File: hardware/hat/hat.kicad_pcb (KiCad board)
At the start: 4 copper layers, 65 x 56 mm, 83 parts, among them J1 GPIO, J2 Uart, J3 LineIn, J4 LineOut, J5 Headphone, U1 CAT24C256, U2 TPS7A20xxxDBV, U3 Oled, U4 MAX98089ETN_T, Y1 12.288MHz

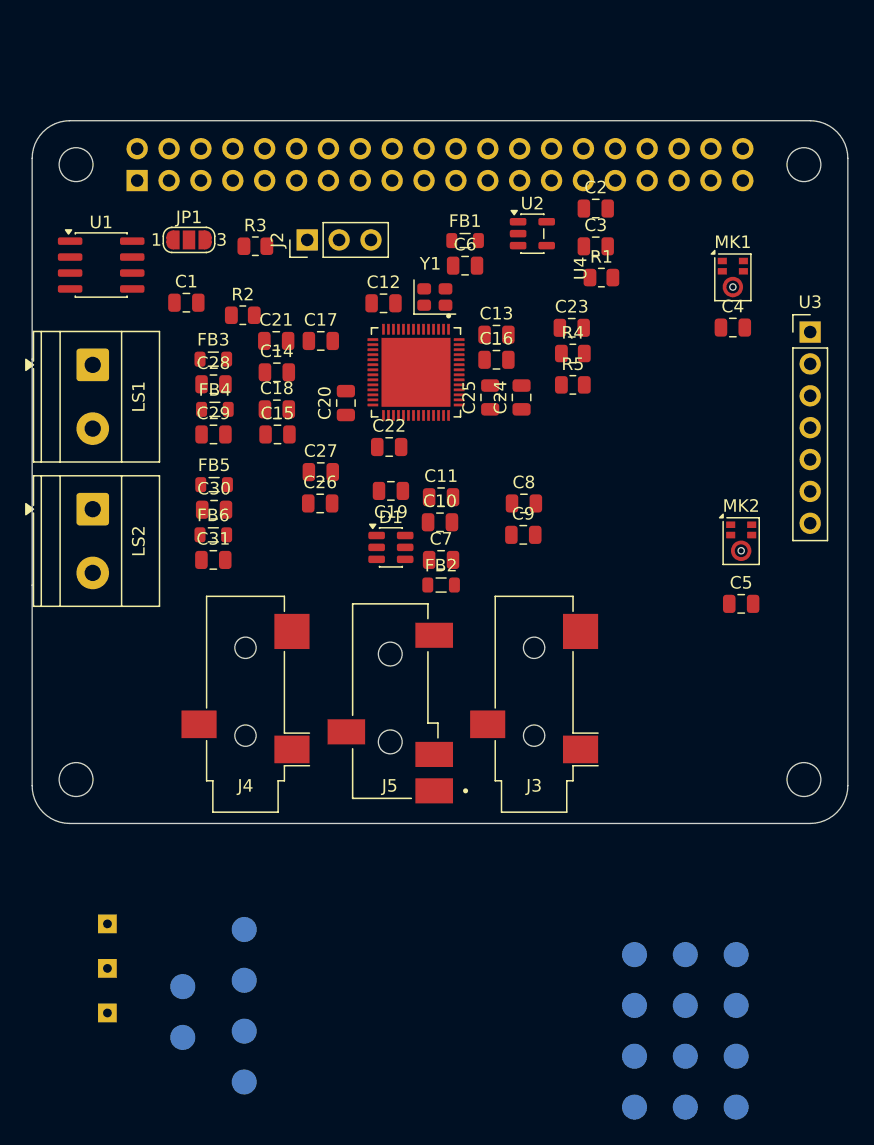
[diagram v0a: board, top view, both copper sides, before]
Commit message: bypass cap
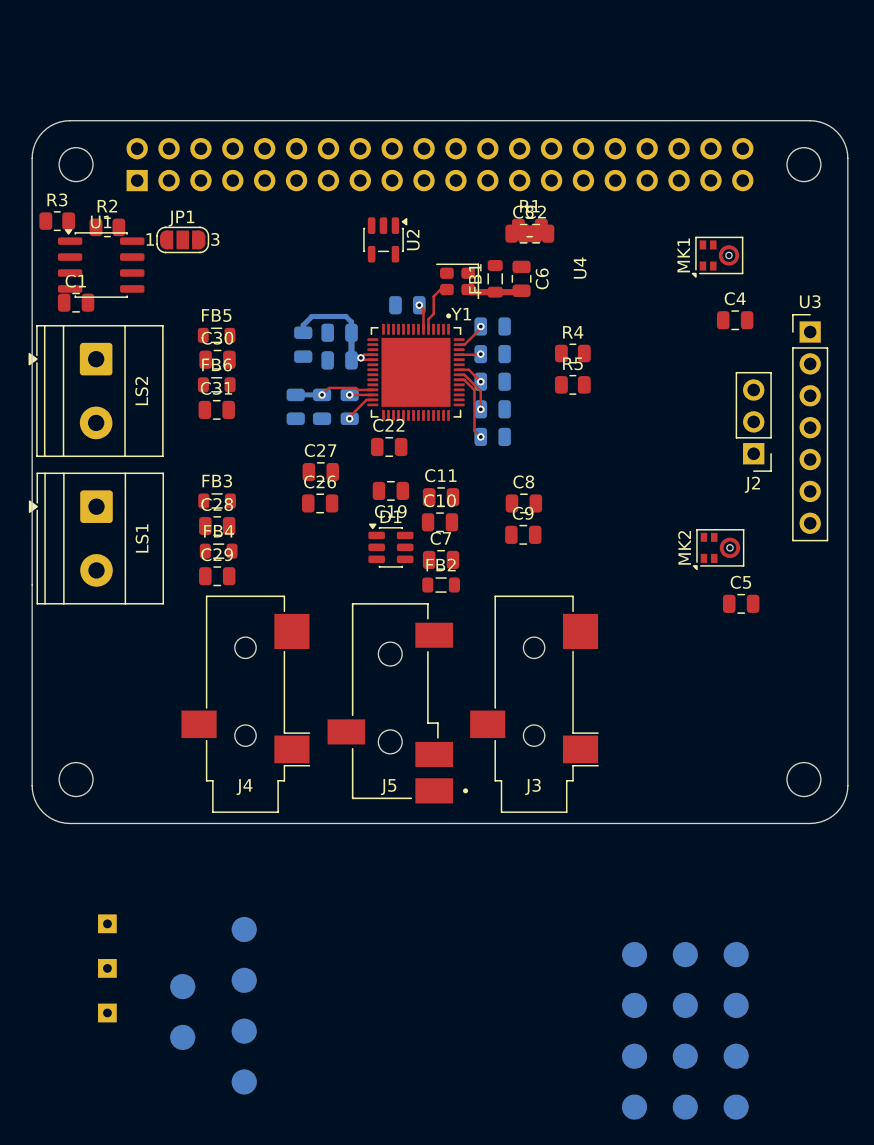
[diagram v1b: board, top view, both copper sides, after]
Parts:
- C12, C13, C14, C15, C16, C17, C18, C20, C21, C23, C24, C25: moved to B.Cu
- moved J2 39.4 mm to (157.5, 70.5), turned to 180 degrees
- moved R3 15.9 mm to (102.0, 52.0)
- moved R2 12.9 mm to (106.0, 52.5)
- moved C30 12.0 mm to (114.8, 63.0)
- moved C31 12.0 mm to (114.7, 67.0)
- moved FB6 12.0 mm to (114.7, 65.0)
- moved LS2 12.0 mm to (105.1, 63.0)
- moved FB5 11.9 mm to (114.7, 61.1)
- moved U2 11.9 mm to (128.0, 53.5), turned to -90 degrees
- moved C28 11.3 mm to (114.8, 76.3)
- moved C29 11.3 mm to (114.8, 80.3)
- moved FB3 11.3 mm to (114.7, 74.3)
- moved FB4 11.3 mm to (114.9, 78.3)
- moved LS1 11.3 mm to (105.1, 74.8)
- moved C1 8.79 mm to (103.5, 58.5)
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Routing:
- net +5V: track 0.00 -> 10.9 mm, vias 0 -> 1
- net +1V8: track 0.00 -> 10.3 mm, vias 0 -> 3
- net Net-(U4-REF): track 0.00 -> 5.50 mm, vias 0 -> 1
- net +3V3: track 0.00 -> 4.47 mm, vias 0 -> 2
- net Net-(Y1-Vcc): track 0.00 -> 4.38 mm
- net Net-(U4-MCLK): track 0.00 -> 4.06 mm
- net Net-(U4-REG): track 0.00 -> 3.72 mm, vias 0 -> 1
- net /codec/C1N: track 0.00 -> 2.56 mm, vias 0 -> 1
- net /codec/C1P: track 0.00 -> 1.85 mm, vias 0 -> 1
- added copper zone on In1.Cu, net GND

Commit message: all signal except ID chip
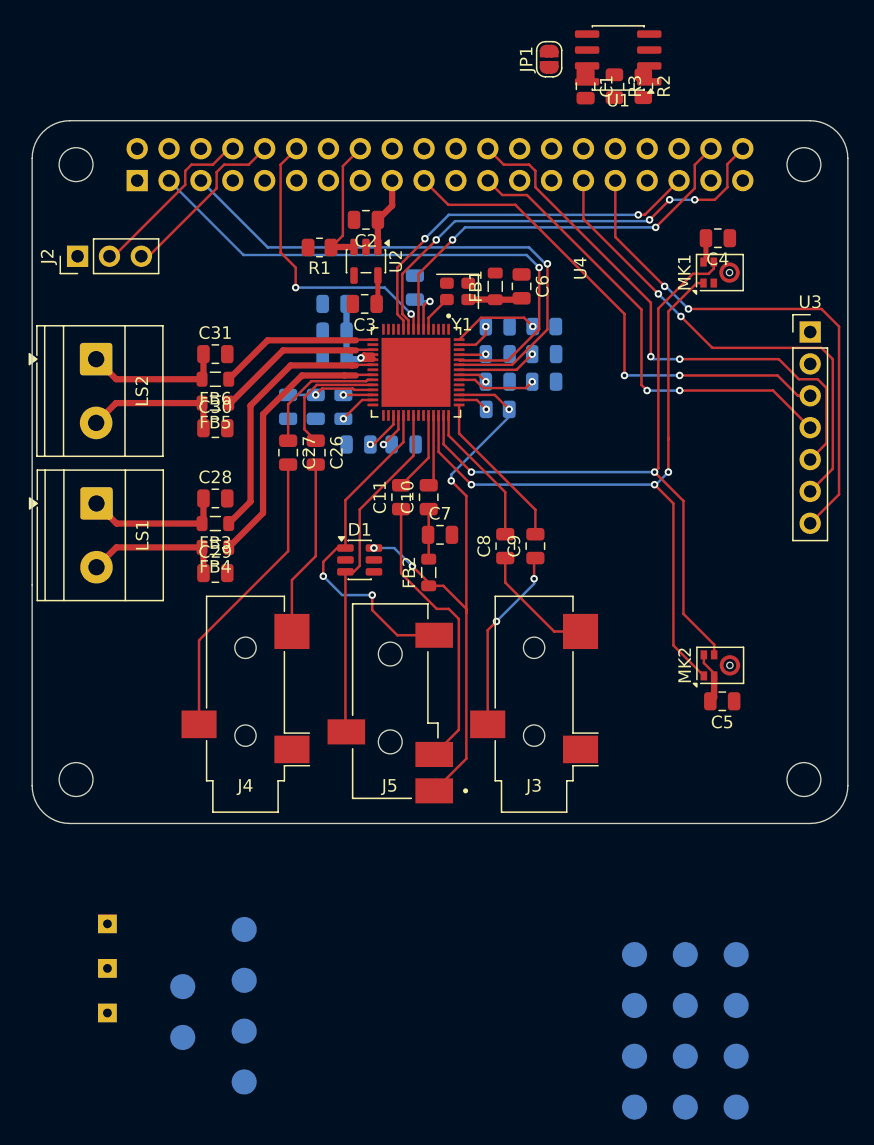
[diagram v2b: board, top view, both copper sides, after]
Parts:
- C19, C22, R4, R5: moved to B.Cu
- JP1: footprint Jumper:SolderJumper-3_P1.3mm_Open_RoundedPad1.0x1.5mm_NumberLabels -> Jumper:SolderJumper-2_P1.3mm_Open_RoundedPad1.0x1.5mm
- moved J2 56.1 mm to (103.6, 54.8), turned to 90 degrees
- moved R3 45.7 mm to (146.4, 41.2), turned to -90 degrees
- moved U1 44.4 mm to (146.7, 39.0), turned to 180 degrees
- moved R2 44.2 mm to (148.7, 41.2), turned to -90 degrees
- moved C1 44.1 mm to (144.1, 41.2), turned to -90 degrees
- moved JP1 32.6 mm to (141.2, 39.1), turned to 90 degrees
- moved R1 16.8 mm to (122.9, 54.1), turned to 180 degrees
- moved C3 13.8 mm to (126.5, 58.6), turned to 180 degrees
- moved C2 13.6 mm to (126.6, 51.9), turned to 180 degrees
- moved MK2 9.36 mm to (154.8, 87.4)
- moved C5 7.91 mm to (155.0, 90.3), turned to 180 degrees
- moved C4 6.68 mm to (154.6, 53.4), turned to 180 degrees
- moved R5 6.30 mm to (137.1, 67.0)
- moved C25 6.01 mm to (140.8, 64.8)
- moved C30 5.46 mm to (114.6, 68.5)
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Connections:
- LS2 pad 1: Net-(C30-Pad1) -> Net-(C31-Pad1)
- LS2 pad 2: Net-(C31-Pad1) -> Net-(C30-Pad1)
- U3 pad 6: /GPIO25 -> /GPIO5
- U3 pad 7: /GPIO27 -> /GPIO6
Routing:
- net /codec/DIGMICDATA: track 0.00 -> 56.1 mm, vias 0 -> 3
- net /codec/DIGMICCLK: track 0.00 -> 56.0 mm, vias 0 -> 2
- net /codec/JackS: track 0.00 -> 48.2 mm, vias 0 -> 4
- net /GPIO2/SDA1: track 0.00 -> 44.7 mm, vias 0 -> 1
- net /GPIO8/SPI0.CE0: track 0.00 -> 44.4 mm, vias 0 -> 2
- net /GPIO3/SCL1: track 0.00 -> 43.8 mm, vias 0 -> 1
- net /GPIO6: track 0.00 -> 41.9 mm, vias 0 -> 2
- net /GPIO10/SPI0.MOSI: track 0.00 -> 40.7 mm, vias 0 -> 2
- net /GPIO5: track 0.00 -> 38.8 mm, vias 0 -> 2
- net /GPIO11/SPI0.SCLK: track 0.00 -> 37.4 mm, vias 0 -> 2
- net /GPIO21/PCM.DOUT: track 0.00 -> 37.0 mm, vias 0 -> 4
- net /GPIO20/PCM.DIN: track 0.00 -> 32.9 mm, vias 0 -> 2
- net /GPIO19/PCM.FS: track 0.00 -> 30.5 mm, vias 0 -> 2
- net Net-(D1-TVS2): track 0.00 -> 27.9 mm
- net Net-(D1-TVS1): track 0.00 -> 27.3 mm, vias 0 -> 2
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
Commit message: all signals
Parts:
- JP1: moved to B.Cu
- moved R2 34.2 mm to (158.3, 74.0)
- moved C1 34.2 mm to (153.7, 74.0)
- moved R3 34.2 mm to (156.0, 74.0)
- moved JP1 33.5 mm to (155.7, 69.3), turned to -90 degrees
- moved U1 31.6 mm to (155.7, 69.3)
- moved C3 4.27 mm to (122.9, 56.3)
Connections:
- Y1 pad 1: /GPIO22 -> /GPIO24
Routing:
- net /ID_SCL: track 0.00 -> 32.0 mm, vias 0 -> 4
- net /ID_SDA: track 0.00 -> 27.0 mm, vias 0 -> 4
- net /GPIO24: track 0.00 -> 14.1 mm
- net +3V3: track 12.3 -> 22.0 mm, vias 2 -> 3
- net Net-(JP1-A): track 0.00 -> 3.01 mm, vias 0 -> 1
- net +1V8: track 24.0 -> 26.2 mm
- net /GPIO11/SPI0.SCLK: track 37.4 -> 36.2 mm
- net /GPIO18/PCM.CLK: track 23.5 -> 24.3 mm
- net /GPIO10/SPI0.MOSI: track 40.7 -> 40.0 mm

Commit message: lil groundfil
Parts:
- removed TP1: MICBIAS, TestPoint:TestPoint_Pad_D2.0mm
- removed TP10: JACKSENSE, TestPoint:TestPoint_Pad_D2.0mm
- removed TP11: RECP, TestPoint:TestPoint_Pad_D2.0mm
- removed TP12: RECN, TestPoint:TestPoint_Pad_D2.0mm
- removed TP13: SPKLP, TestPoint:TestPoint_Pad_D2.0mm
- removed TP14: SPKLN, TestPoint:TestPoint_Pad_D2.0mm
- removed TP15: SPKRP, TestPoint:TestPoint_Pad_D2.0mm
- removed TP16: SPKRN, TestPoint:TestPoint_Pad_D2.0mm
- removed TP17: LDO_IN, TestPoint:TestPoint_Pad_D2.0mm
- removed TP18: LDO_OUT, TestPoint:TestPoint_Pad_D2.0mm
- removed TP19: 5V, TestPoint:TestPoint_THTPad_1.5x1.5mm_Drill0.7mm
- removed TP2: INA1, TestPoint:TestPoint_Pad_D2.0mm
- removed TP20: GND, TestPoint:TestPoint_THTPad_1.5x1.5mm_Drill0.7mm
- removed TP21: 3V3, TestPoint:TestPoint_THTPad_1.5x1.5mm_Drill0.7mm
- removed TP3: INA2, TestPoint:TestPoint_Pad_D2.0mm
- removed TP4: CODEC_MCLK, TestPoint:TestPoint_Pad_D2.0mm
- removed TP5: MIC2P, TestPoint:TestPoint_Pad_D2.0mm
- removed TP6: MIC2N, TestPoint:TestPoint_Pad_D2.0mm
- removed TP7: HPSNS, TestPoint:TestPoint_Pad_D2.0mm
- removed TP8: HPR, TestPoint:TestPoint_Pad_D2.0mm
- removed TP9: HPL, TestPoint:TestPoint_Pad_D2.0mm
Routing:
- added copper zone on In2.Cu, net +3V3
- added copper zone on In2.Cu, net +5V

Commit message: some troll power planes
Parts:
- moved R3 15.0 mm to (148.6, 61.0), turned to 180 degrees
- moved R2 14.6 mm to (148.6, 63.1), turned to 180 degrees
- moved C1 11.8 mm to (143.6, 68.0), turned to 90 degrees
- moved U3 9.70 mm to (156.3, 68.7), turned to 180 degrees
- moved C4 8.61 mm to (162.1, 57.8)
- moved MK1 8.44 mm to (162.0, 60.5)
- moved MK2 7.73 mm to (162.0, 84.5)
- moved C5 7.72 mm to (162.1, 87.2)
- moved JP1 7.42 mm to (148.6, 67.1)
- moved U1 7.42 mm to (148.6, 67.1)
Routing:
- net /GPIO6: track 41.9 -> 13.2 mm, vias 2 -> 0
- net /GPIO5: track 38.8 -> 16.1 mm, vias 2 -> 0
- net /GPIO8/SPI0.CE0: track 44.8 -> 25.8 mm, vias 2 -> 0
- net /GPIO11/SPI0.SCLK: track 36.2 -> 25.1 mm, vias 2 -> 0
- net /GPIO10/SPI0.MOSI: track 40.0 -> 31.3 mm, vias 2 -> 0
- net /ID_SDA: track 27.0 -> 19.7 mm, vias 4 -> 2
- net /ID_SCL: track 32.0 -> 24.9 mm, vias 4 -> 2
- net +3V3: track 22.0 -> 29.1 mm
- added copper zone on In2.Cu, net +1V8

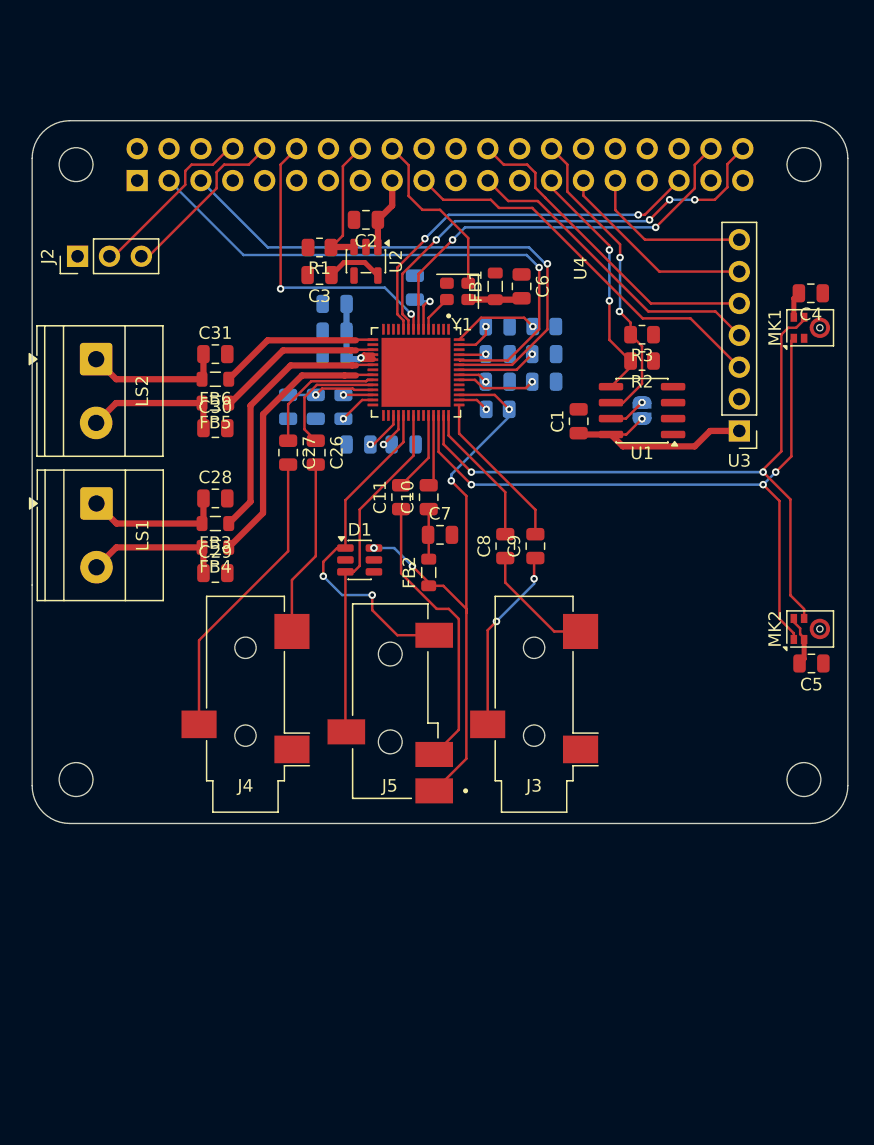
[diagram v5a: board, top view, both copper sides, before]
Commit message: vias for planes
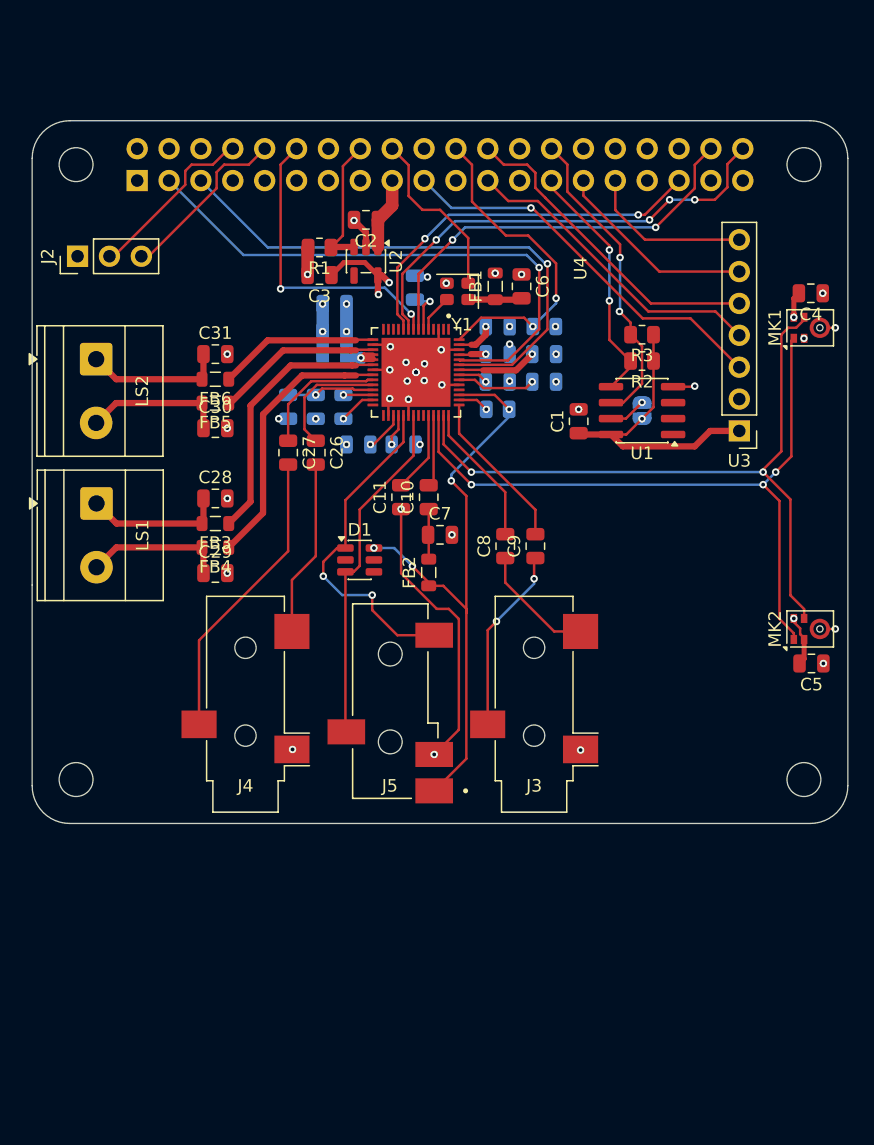
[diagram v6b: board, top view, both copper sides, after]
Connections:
- R4 pad 1: /GPIO17 -> /GPIO25
- U4 pad 56: /GPIO17 -> /GPIO25
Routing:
- net GND: track 22.8 -> 63.7 mm, vias 0 -> 44
- net /GPIO25: track 0.00 -> 26.2 mm, vias 0 -> 2
- net +3V3: track 29.1 -> 36.2 mm, vias 3 -> 5
- net /GPIO17: track 6.89 -> 0.00 mm, vias 1 -> 0
- net +1V8: track 26.2 -> 33.1 mm, vias 3 -> 7
- net +5V: track 8.03 -> 12.4 mm, vias 1 -> 3
- net Net-(U4-HPVDD): track 3.46 -> 2.54 mm
- net /GPIO10/SPI0.MOSI: vias 0 -> 1

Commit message: before drc
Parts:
- added TP1: MICBIAS, TestPoint:TestPoint_Pad_D2.0mm, F.Cu at (147.4, 97.5)
- added TP10: JACKSENSE, TestPoint:TestPoint_Pad_D2.0mm, F.Cu at (140.7, 67.6)
- added TP11: RECP, TestPoint:TestPoint_Pad_D2.0mm, F.Cu at (109.3, 85.1)
- added TP12: RECN, TestPoint:TestPoint_Pad_D2.0mm, F.Cu at (109.2, 88.5)
- added TP13: SPKLP, TestPoint:TestPoint_Pad_D2.0mm, F.Cu at (115.5, 71.4)
- added TP14: SPKLN, TestPoint:TestPoint_Pad_D2.0mm, F.Cu at (118.5, 77.8)
- added TP15: SPKRP, TestPoint:TestPoint_Pad_D2.0mm, F.Cu at (112.5, 71.5)
- added TP16: SPKRN, TestPoint:TestPoint_Pad_D2.0mm, F.Cu at (113.7, 60.0)
- added TP17: LDO_IN, TestPoint:TestPoint_Pad_D2.0mm, F.Cu at (122.4, 51.5)
- added TP18: LDO_OUT, TestPoint:TestPoint_Pad_D2.0mm, F.Cu at (120.8, 59.5)
- added TP19: 5V, TestPoint:TestPoint_THTPad_1.5x1.5mm_Drill0.7mm, F.Cu at (113.7, 53.6)
- added TP2: INA1, TestPoint:TestPoint_Pad_D2.0mm, F.Cu at (143.5, 79.0)
- added TP20: GND, TestPoint:TestPoint_THTPad_1.5x1.5mm_Drill0.7mm, F.Cu at (113.7, 56.4)
- added TP3: INA2, TestPoint:TestPoint_Pad_D2.0mm, F.Cu at (146.8, 79.0)
- added TP4: CODEC_MCLK, TestPoint:TestPoint_Pad_D2.0mm, F.Cu at (136.2, 53.8)
- added TP5: MIC2P, TestPoint:TestPoint_Pad_D2.0mm, F.Cu at (125.5, 72.6)
- added TP6: MIC2N, TestPoint:TestPoint_Pad_D2.0mm, F.Cu at (124.3, 75.5)
- added TP7: HPSNS, TestPoint:TestPoint_Pad_D2.0mm, F.Cu at (109.4, 92.0)
- added TP8: HPR, TestPoint:TestPoint_Pad_D2.0mm, F.Cu at (109.4, 95.2)
- added TP9: HPL, TestPoint:TestPoint_Pad_D2.0mm, F.Cu at (109.4, 98.2)
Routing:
- net Net-(D1-TVS1): track 27.3 -> 60.5 mm
- net Net-(D1-TVS2): track 27.9 -> 47.1 mm
- net /codec/JackS: track 48.2 -> 63.6 mm
- net GND: track 63.7 -> 75.9 mm
- net Net-(C26-Pad2): track 14.1 -> 26.3 mm, vias 0 -> 2
- net Net-(U4-MIC2N): track 12.8 -> 22.6 mm
- net Net-(U4-MIC2P): track 11.3 -> 19.7 mm
- net Net-(U4-INA1/EXTMICP): track 5.73 -> 13.1 mm, vias 0 -> 2
- net Net-(U4-MCLK): track 2.97 -> 9.65 mm, vias 0 -> 2
- net Net-(U4-INA2/EXTMICN): track 6.47 -> 12.6 mm, vias 0 -> 2
- net +3V3: track 36.2 -> 42.3 mm, vias 5 -> 7
- net Net-(C29-Pad1): track 11.2 -> 16.8 mm
- net Net-(C27-Pad2): track 23.6 -> 28.4 mm
- net +1V8: track 33.1 -> 37.5 mm
- net Net-(C28-Pad1): track 11.1 -> 14.6 mm
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
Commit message: done?
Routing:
- net +1V8: track 37.5 -> 34.9 mm
- net +5V: track 12.4 -> 10.2 mm
- net Net-(U4-SPKLN): track 22.7 -> 21.8 mm
- net GND: vias 44 -> 43
- added copper zone on F.Cu, net +5V
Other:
- board text added: "GND TX RX"
